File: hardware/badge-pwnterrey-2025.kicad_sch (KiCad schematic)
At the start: 16 parts, among them J1 Conn_01x04_Socket, SW1 SW_RST, SW2 On, U1 PY32F002AA15M6TU

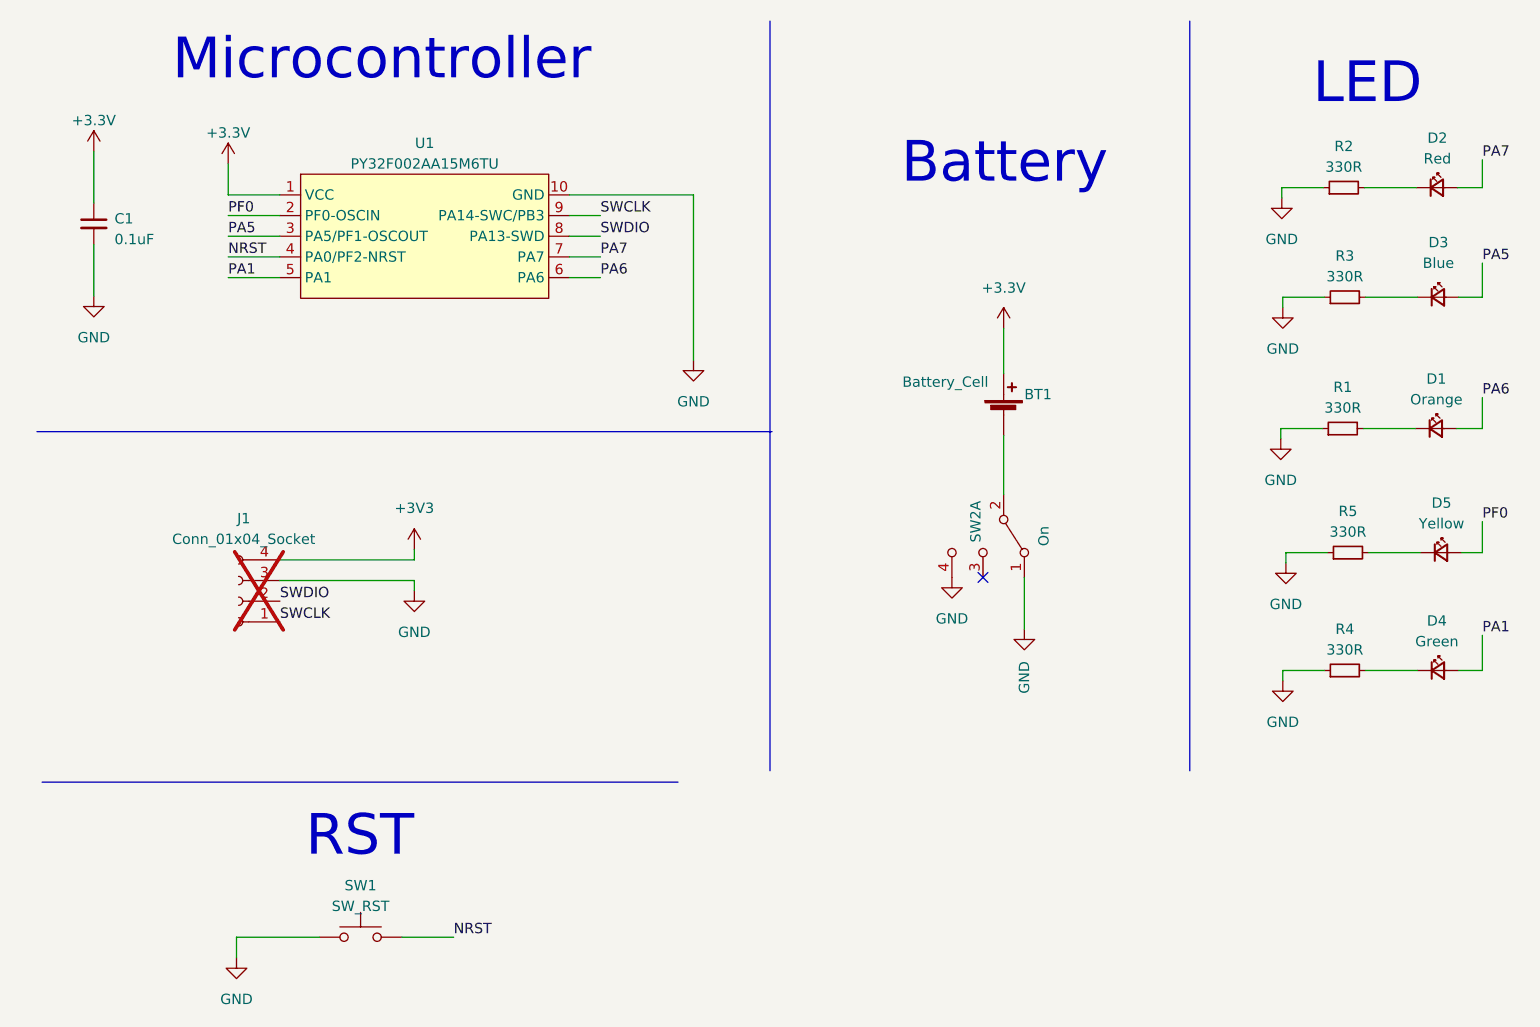
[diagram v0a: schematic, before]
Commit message: feat(hw): add floorplan
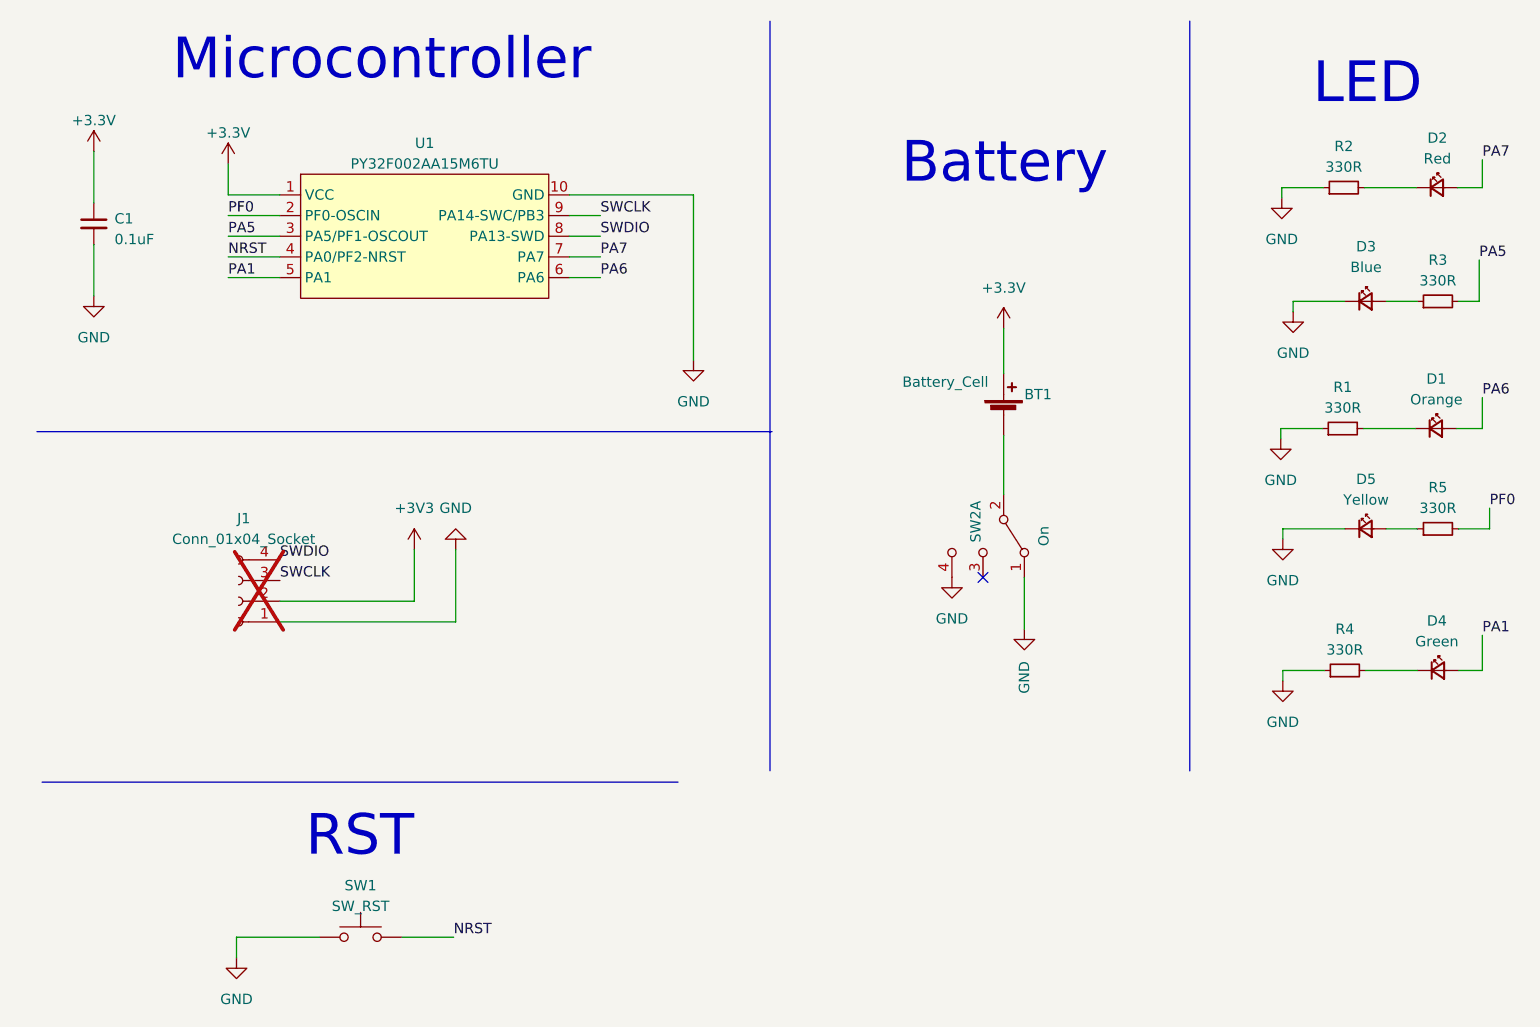
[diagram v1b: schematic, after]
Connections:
- net +3V3: now also J1.2 (Pin_2); no longer J1.4 (Pin_4)
- net GND: now also D3.1 (K), D5.1 (K), J1.1 (Pin_1); no longer J1.3 (Pin_3), R3.1, R5.1
- net PA5: now also R3.2; no longer D3.2 (A)
- net PF0: now also R5.2; no longer D5.2 (A)
- net SWCLK: now also J1.3 (Pin_3); no longer J1.1 (Pin_1)
- net SWDIO: now also J1.4 (Pin_4); no longer J1.2 (Pin_2)
- new net: D5.2 (A), R5.1
- new net: D3.2 (A), R3.1
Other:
- moved on the sheet: D3, D5, R3, R5

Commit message: feat(hw): add routes
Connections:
- net +3V3 is gone; now on net +3.3V: J1.2 (Pin_2)
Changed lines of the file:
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@@
-	)
-	(symbol
-		(lib_id "power:+3V3")
-		(at 59.69 77.47 0)
-		(unit 1)
-		(exclude_from_sim no)
-		(in_bom yes)
-		(on_board yes)
-		(dnp no)
-		(fields_autoplaced yes)
-		(property "Reference" "#PWR06"
-			(at 59.69 81.28 0)
-			(effects
-				(font
-					(size 1.27 1.27)
-				)
-				(hide yes)
-			)
-		)
-		(property "Value" "+3V3"
-			(at 59.69 72.39 0)
-			(effects
-				(font
-					(size 1.27 1.27)
-				)
-			)
-		)
-		(property "Footprint" ""
-			(at 59.69 77.47 0)
-			(effects
-				(font
-					(size 1.27 1.27)
-				)
-				(hide yes)
-			)
-		)
-		(property "Datasheet" ""
-			(at 59.69 77.47 0)
-			(effects
-				(font
-					(size 1.27 1.27)
-				)
-				(hide yes)
-			)
-		)
-		(property "Description" "Power symbol creates a global label with name \"+3V3\""
-			(at 59.69 77.47 0)
-			(effects
-				(font
-					(size 1.27 1.27)
-				)
-				(hide yes)
-			)
-		)
-		(pin "1"
-		)
-		(instances
-			(project ""
-				(path "/85de002e-ba9e-4d97-83b6-4373a73752cf"
-					(reference "#PWR06")
-					(unit 1)
-				)
-			)
-		)
 	)
 	(symbol
@@
 					(unit 1)
 				)
+			)
+		)
+	)
+	(symbol
+		(lib_name "+3.3V_1")
+		(lib_id "power:+3.3V")
+		(at 59.69 77.47 0)
+		(unit 1)
+		(exclude_from_sim no)
+		(in_bom yes)
+		(on_board yes)
+		(dnp no)
+		(fields_autoplaced yes)
+		(property "Reference" "#PWR06"
+			(at 59.69 81.28 0)
+			(effects
+				(font
+					(size 1.27 1.27)
+				)
+				(hide yes)
+			)
+		)
+		(property "Value" "+3.3V"
+			(at 59.69 72.39 0)
+			(effects
+				(font
+					(size 1.27 1.27)
+				)
+			)
+		)
+		(property "Footprint" ""
+			(at 59.69 77.47 0)
+			(effects
+				(font
+					(size 1.27 1.27)
+				)
+				(hide yes)
+			)
+		)
+		(property "Datasheet" ""
+			(at 59.69 77.47 0)
+			(effects
+				(font
+					(size 1.27 1.27)
+				)
+				(hide yes)
+			)
+		)
+		(property "Description" "Power symbol creates a global label with name \"+3.3V\""
+			(at 59.69 77.47 0)
+			(effects
+				(font
+					(size 1.27 1.27)
+				)
+				(hide yes)
+			)
+		)
+		(pin "1"
+		)
+		(instances
+			(project ""
+				(path "/85de002e-ba9e-4d97-83b6-4373a73752cf"
+					(reference "#PWR06")
+					(unit 1)
+				)

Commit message: feat(Hw):Added_Labels
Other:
- company: (none) -> ElectronicCats
- title: (none) -> PWNterrey
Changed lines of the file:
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@@
 	(generator_version "9.0")
 	(paper "A5")
+	(title_block
+		(title "PWNterrey")
+		(date "2025-03-14")
+		(rev "v1.0")
+		(company "ElectronicCats")
+		(comment 1 "Adonai Diaz")
+	)
 	(text "LED\n"
 		(exclude_from_sim no)
@@
 	(polyline
 		(pts
-			(xy 13.97 106.045) (xy 92.075 106.045)
-		)
-		(stroke
+			(xy 10.795 106.68) (xy 88.9 106.68)
+		)
+		(stroke
